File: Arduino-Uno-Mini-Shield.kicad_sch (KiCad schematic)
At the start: 8 parts, among them J2 Conn_01x06, J3 Conn_01x08, J4 Conn_01x08, J5 Conn_01x10

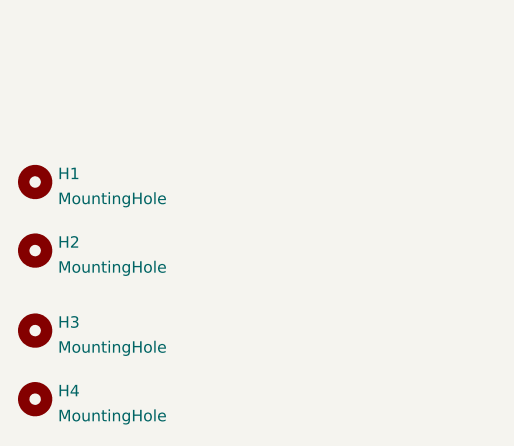
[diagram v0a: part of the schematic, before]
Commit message: final changes
added VIAS as mounting holes
added GND fill
added +5V connection
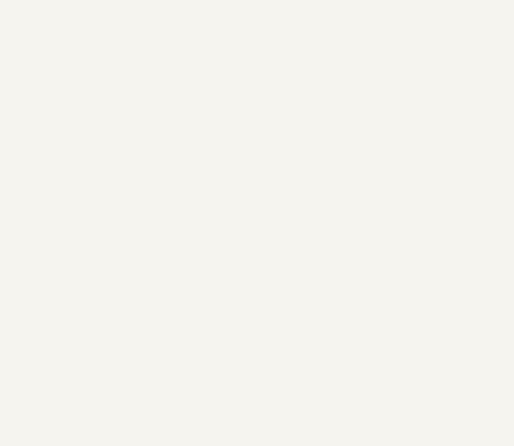
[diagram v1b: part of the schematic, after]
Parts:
- removed H1, H2, H3, H4: MountingHole, symbol Mechanical:MountingHole
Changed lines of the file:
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@@
     (effects (font (size 1.27 1.27)) (justify left bottom))
-  )
-  (symbol (lib_id "Mechanical:MountingHole") (at 73.66 161.29 0) (unit 1)
-    (in_bom yes) (on_board yes) (fields_autoplaced)
-    (property "Reference" "H2" (id 0) (at 76.2 160.3815 0)
-      (effects (font (size 1.27 1.27)) (justify left))
-    )
-    (property "Value" "MountingHole" (id 1) (at 76.2 163.1566 0)
-      (effects (font (size 1.27 1.27)) (justify left))
-    )
-    (property "Footprint" "" (id 2) (at 73.66 161.29 0)
-      (effects (font (size 1.27 1.27)) hide)
-    )
-    (property "Datasheet" "~" (id 3) (at 73.66 161.29 0)
-      (effects (font (size 1.27 1.27)) hide)
-    )
   )
   (symbol (lib_id "Connector_Generic:Conn_01x06") (at 220.98 62.23 0) (unit 1)
@@
     (pin "9")
   )
-  (symbol (lib_id "Mechanical:MountingHole") (at 73.66 153.67 0) (unit 1)
-    (in_bom yes) (on_board yes) (fields_autoplaced)
-    (property "Reference" "H1" (id 0) (at 76.2 152.7615 0)
-      (effects (font (size 1.27 1.27)) (justify left))
-    )
-    (property "Value" "MountingHole" (id 1) (at 76.2 155.5366 0)
-      (effects (font (size 1.27 1.27)) (justify left))
-    )
-    (property "Footprint" "" (id 2) (at 73.66 153.67 0)
-      (effects (font (size 1.27 1.27)) hide)
-    )
-    (property "Datasheet" "~" (id 3) (at 73.66 153.67 0)
-      (effects (font (size 1.27 1.27)) hide)
-    )
-  )
   (symbol (lib_id "Connector_Generic:Conn_01x08") (at 220.98 87.63 0) (mirror x) (unit 1)
     (in_bom yes) (on_board yes) (fields_autoplaced)
@@
     (pin "8")
   )
-  (symbol (lib_id "Mechanical:MountingHole") (at 73.66 177.8 0) (unit 1)
-    (in_bom yes) (on_board yes) (fields_autoplaced)
-    (property "Reference" "H4" (id 0) (at 76.2 176.8915 0)
-      (effects (font (size 1.27 1.27)) (justify left))
-    )
-    (property "Value" "MountingHole" (id 1) (at 76.2 179.6666 0)
-      (effects (font (size 1.27 1.27)) (justify left))
-    )
-    (property "Footprint" "" (id 2) (at 73.66 177.8 0)
-      (effects (font (size 1.27 1.27)) hide)
-    )
-    (property "Datasheet" "~" (id 3) (at 73.66 177.8 0)
-      (effects (font (size 1.27 1.27)) hide)
-    )
-  )
-  (symbol (lib_id "Mechanical:MountingHole") (at 73.66 170.18 0) (unit 1)
-    (in_bom yes) (on_board yes) (fields_autoplaced)
-    (property "Reference" "H3" (id 0) (at 76.2 169.2715 0)
-      (effects (font (size 1.27 1.27)) (justify left))
-    )
-    (property "Value" "MountingHole" (id 1) (at 76.2 172.0466 0)
-      (effects (font (size 1.27 1.27)) (justify left))
-    )
-    (property "Footprint" "" (id 2) (at 73.66 170.18 0)
-      (effects (font (size 1.27 1.27)) hide)
-    )
-    (property "Datasheet" "~" (id 3) (at 73.66 170.18 0)
-      (effects (font (size 1.27 1.27)) hide)
-    )
-  )
   (sheet_instances
     (path "/" (page "1"))
   )
   (symbol_instances
-    (path "/a14dc353-9f8d-4bb2-98a1-d0ab808a1f55"
-      (reference "H1") (unit 1) (value "MountingHole") (footprint "")
-    )
-    (path "/180c293a-551f-480b-9d78-eeb8cb42b3a7"
-      (reference "H2") (unit 1) (value "MountingHole") (footprint "")
-    )
-    (path "/e85e7b53-fc27-4677-abdf-c28b2ca07cfc"
-      (reference "H3") (unit 1) (value "MountingHole") (footprint "")
-    )
-    (path "/c243bb80-29d6-4595-bdc4-e0e51f62b9c4"
-      (reference "H4") (unit 1) (value "MountingHole") (footprint "")
-    )
     (path "/467b4061-0036-4f37-bc11-2c9e5580407c"
       (reference "J2") (unit 1) (value "Conn_01x06") (footprint "Connector_PinHeader_1.27mm:PinHeader_1x06_P1.27mm_Vertical")
